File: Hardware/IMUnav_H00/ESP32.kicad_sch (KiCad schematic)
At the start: 16 parts

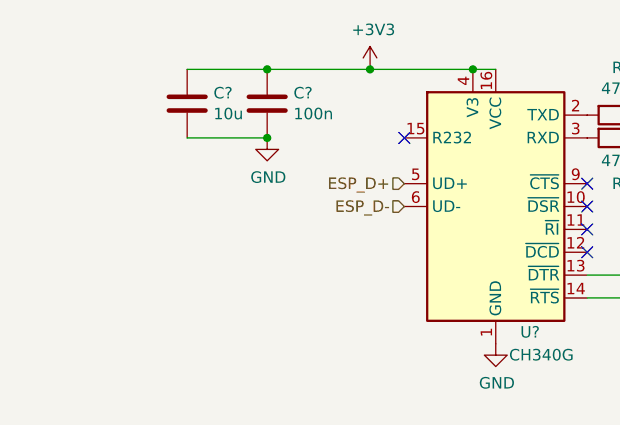
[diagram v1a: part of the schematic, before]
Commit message: Added GPS. Changes in power management.
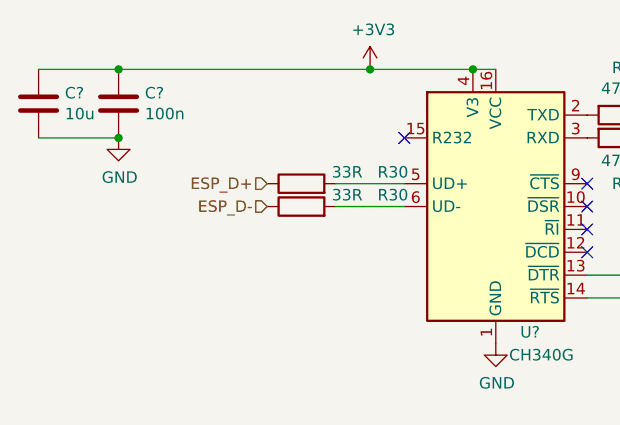
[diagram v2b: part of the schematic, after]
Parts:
- added R30 (x2): 33R, Resistor_SMD:R_0603_1608Metric, symbol Device:R
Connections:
- net ESP_D+: now also R30.1; no longer U?.5 (UD+)
- net ESP_D-: now also R30.1; no longer U?.6 (UD-)
- new net: R30.2, U?.5 (UD+)
- new net: R30.2, U?.6 (UD-)
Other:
- moved on the sheet: C?
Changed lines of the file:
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@@
   (junction (at 137.16 67.31) (diameter 0) (color 0 0 0 0)
   )
-  (junction (at 88.9 41.91) (diameter 0) (color 0 0 0 0)
+  (junction (at 72.39 41.91) (diameter 0) (color 0 0 0 0)
   )
   (junction (at 111.76 41.91) (diameter 0) (color 0 0 0 0)
@@
   (junction (at 120.65 99.06) (diameter 0) (color 0 0 0 0)
   )
-  (junction (at 88.9 49.53) (diameter 0) (color 0 0 0 0)
+  (junction (at 72.39 49.53) (diameter 0) (color 0 0 0 0)
   )
   (junction (at 120.65 105.41) (diameter 0) (color 0 0 0 0)
@@
     (stroke (width 0) (type default))
   )
+  (wire (pts (xy 96.52 57.15) (xy 104.14 57.15))
+    (stroke (width 0) (type default))
+  )
   (wire (pts (xy 177.8 41.91) (xy 177.8 119.38))
     (stroke (width 0) (type default))
@@
     (stroke (width 0) (type default))
   )
-  (wire (pts (xy 88.9 41.91) (xy 100.33 41.91))
+  (wire (pts (xy 72.39 41.91) (xy 100.33 41.91))
     (stroke (width 0) (type default))
   )
@@
     (stroke (width 0) (type default))
   )
-  (wire (pts (xy 88.9 49.53) (xy 80.01 49.53))
+  (wire (pts (xy 72.39 49.53) (xy 63.5 49.53))
     (stroke (width 0) (type default))
   )
@@
     (stroke (width 0) (type default))
   )
-  (wire (pts (xy 80.01 41.91) (xy 88.9 41.91))
+  (wire (pts (xy 63.5 41.91) (xy 72.39 41.91))
     (stroke (width 0) (type default))
   )
@@
   )
   (wire (pts (xy 120.65 99.06) (xy 120.65 105.41))
+    (stroke (width 0) (type default))
+  )
+  (wire (pts (xy 96.52 54.61) (xy 104.14 54.61))
     (stroke (width 0) (type default))
   )
@@
     (effects (font (size 1.27 1.27)) (justify left))
   )
-  (hierarchical_label "ESP_D+" (shape input) (at 104.14 54.61 180) (fields_autoplaced)
+  (hierarchical_label "ESP_D+" (shape input) (at 88.9 54.61 180) (fields_autoplaced)
     (effects (font (size 1.27 1.27)) (justify right))
   )
@@
     (effects (font (size 1.27 1.27)) (justify left))
   )
-  (hierarchical_label "ESP_D-" (shape input) (at 104.14 57.15 180) (fields_autoplaced)
+  (hierarchical_label "ESP_D-" (shape input) (at 88.9 57.15 180) (fields_autoplaced)
     (effects (font (size 1.27 1.27)) (justify right))
   )
@@
     )
   )
+  (symbol (lib_id "Device:R") (at 92.71 54.61 90) (unit 1)
+    (in_bom yes) (on_board yes) (dnp no)
+    (property "Reference" "R30" (at 102.87 53.34 90)
+      (effects (font (size 1.27 1.27)))
+    )
+    (property "Value" "33R" (at 97.79 53.34 90)
+      (effects (font (size 1.27 1.27)))
+    )
+    (property "Footprint" "Resistor_SMD:R_0603_1608Metric" (at 92.71 56.388 90)
+      (effects (font (size 1.27 1.27)) hide)
+    )
+    (property "Datasheet" "~" (at 92.71 54.61 0)
+      (effects (font (size 1.27 1.27)) hide)
+    )
+    (property "LCSC" "C23140" (at 92.71 54.61 90)
+      (effects (font (size 1.27 1.27)) hide)
+    )
+    (pin "1")
+    (pin "2")
+    (instances
+      (project "IMUnav_H00"
+        (path "/4c2dd95e-3649-4040-ab57-00df6d22e0b0/368409dd-4d9a-4752-893d-5939a8c78734"
+          (reference "R30") (unit 1)
+        )
+        (path "/4c2dd95e-3649-4040-ab57-00df6d22e0b0/61a7e487-220c-46a1-aef5-176736fd02e1"
+          (reference "R32") (unit 1)
+        )
+        (path "/4c2dd95e-3649-4040-ab57-00df6d22e0b0/bf35eb2a-37f7-4f5f-b34e-af3028cdd96b"
+          (reference "R34") (unit 1)
+        )
+      )
+    )
+  )
   (symbol (lib_id "power:GND") (at 114.3 72.39 0) (unit 1)
     (in_bom yes) (on_board yes) (dnp no)
@@
         (path "/68867493-9f89-4388-916e-56f5ada0ac5c/4ec8e228-d742-4cd8-8c0d-36879b06f45c"
           (reference "Q?") (unit 1)
+        )
+      )
+    )
+  )
+  (symbol (lib_id "Device:R") (at 92.71 57.15 90) (unit 1)
+    (in_bom yes) (on_board yes) (dnp no)
+    (property "Reference" "R30" (at 102.87 55.88 90)
+      (effects (font (size 1.27 1.27)))
+    )
+    (property "Value" "33R" (at 97.79 55.88 90)
+      (effects (font (size 1.27 1.27)))
+    )
+    (property "Footprint" "Resistor_SMD:R_0603_1608Metric" (at 92.71 58.928 90)
+      (effects (font (size 1.27 1.27)) hide)
+    )
+    (property "Datasheet" "~" (at 92.71 57.15 0)
+      (effects (font (size 1.27 1.27)) hide)
+    )
+    (property "LCSC" "C23140" (at 92.71 57.15 90)
+      (effects (font (size 1.27 1.27)) hide)
+    )
+    (pin "1")
+    (pin "2")
+    (instances
+      (project "IMUnav_H00"
+        (path "/4c2dd95e-3649-4040-ab57-00df6d22e0b0/368409dd-4d9a-4752-893d-5939a8c78734"
+          (reference "R30") (unit 1)
+        )
+        (path "/4c2dd95e-3649-4040-ab57-00df6d22e0b0/61a7e487-220c-46a1-aef5-176736fd02e1"
+          (reference "R32") (unit 1)
+        )
+        (path "/4c2dd95e-3649-4040-ab57-00df6d22e0b0/bf35eb2a-37f7-4f5f-b34e-af3028cdd96b"
+          (reference "R35") (unit 1)
         )
       )
@@
     )
   )
-  (symbol (lib_id "power:GND") (at 88.9 49.53 0) (unit 1)
-    (in_bom yes) (on_board yes) (dnp no)
-    (property "Reference" "#PWR?" (at 88.9 55.88 0)
-      (effects (font (size 1.27 1.27)) hide)
-    )
-    (property "Value" "GND" (at 89.027 53.9242 0)
-      (effects (font (size 1.27 1.27)))
-    )
-    (property "Footprint" "" (at 88.9 49.53 0)
-      (effects (font (size 1.27 1.27)) hide)
-    )
-    (property "Datasheet" "" (at 88.9 49.53 0)
+  (symbol (lib_id "power:GND") (at 72.39 49.53 0) (unit 1)
+    (in_bom yes) (on_board yes) (dnp no)
+    (property "Reference" "#PWR?" (at 72.39 55.88 0)
+      (effects (font (size 1.27 1.27)) hide)
+    )
+    (property "Value" "GND" (at 72.517 53.9242 0)
+      (effects (font (size 1.27 1.27)))
+    )
+    (property "Footprint" "" (at 72.39 49.53 0)
+      (effects (font (size 1.27 1.27)) hide)
+    )
+    (property "Datasheet" "" (at 72.39 49.53 0)
       (effects (font (size 1.27 1.27)) hide)
     )
@@
     )
   )
-  (symbol (lib_id "Device:C") (at 80.01 45.72 0) (unit 1)
-    (in_bom yes) (on_board yes) (dnp no)
-    (property "Reference" "C?" (at 82.931 44.5516 0)
-      (effects (font (size 1.27 1.27)) (justify left))
-    )
-    (property "Value" "10u" (at 82.931 46.863 0)
-      (effects (font (size 1.27 1.27)) (justify left))
-    )
-    (property "Footprint" "Capacitor_SMD:C_0603_1608Metric" (at 80.9752 49.53 0)
-      (effects (font (size 1.27 1.27)) hide)
-    )
-    (property "Datasheet" "~" (at 80.01 45.72 0)
-      (effects (font (size 1.27 1.27)) hide)
-    )
-    (property "LCSC" "C19702" (at 80.01 45.72 0)
+  (symbol (lib_id "Device:C") (at 63.5 45.72 0) (unit 1)
+    (in_bom yes) (on_board yes) (dnp no)
+    (property "Reference" "C?" (at 66.421 44.5516 0)
+      (effects (font (size 1.27 1.27)) (justify left))
+    )
+    (property "Value" "10u" (at 66.421 46.863 0)
+      (effects (font (size 1.27 1.27)) (justify left))
+    )
+    (property "Footprint" "Capacitor_SMD:C_0603_1608Metric" (at 64.4652 49.53 0)
+      (effects (font (size 1.27 1.27)) hide)
+    )
+    (property "Datasheet" "~" (at 63.5 45.72 0)
+      (effects (font (size 1.27 1.27)) hide)
+    )
+    (property "LCSC" "C19702" (at 63.5 45.72 0)
       (effects (font (size 1.27 1.27)) hide)
     )
@@
     )
   )
-  (symbol (lib_id "Device:C") (at 88.9 45.72 0) (unit 1)
-    (in_bom yes) (on_board yes) (dnp no)
-    (property "Reference" "C?" (at 91.821 44.5516 0)
-      (effects (font (size 1.27 1.27)) (justify left))
-    )
-    (property "Value" "100n" (at 91.821 46.863 0)
-      (effects (font (size 1.27 1.27)) (justify left))
-    )
-    (property "Footprint" "Capacitor_SMD:C_0603_1608Metric" (at 89.8652 49.53 0)
-      (effects (font (size 1.27 1.27)) hide)
-    )
-    (property "Datasheet" "~" (at 88.9 45.72 0)
-      (effects (font (size 1.27 1.27)) hide)
-    )
-    (property "LCSC" "C14663" (at 88.9 45.72 0)
-      (effects (font (size 1.27 1.27)) hide)
-    )
+  (symbol (lib_id "Device:C") (at 72.39 45.72 0) (unit 1)
+    (in_bom yes) (on_board yes) (dnp no)
+    (property "Reference" "C?" (at 75.311 44.5516 0)
+      (effects (font (size 1.27 1.27)) (justify left))
+    )
+    (property "Value" "100n" (at 75.311 46.863 0)
+      (effects (font (size 1.27 1.27)) (justify left))
+    )
+    (property "Footprint" "Capacitor_SMD:C_0603_1608Metric" (at 73.3552 49.53 0)
+      (effects (font (size 1.27 1.27)) hide)
+    )
+    (property "Datasheet" "~" (at 72.39 45.72 0)
+      (effects (font (size 1.27 1.27)) hide)
+    )
+    (property "LCSC" "C14663" (at 72.39 45.72 0)
+      (effects (font (size 1.27 1.27)) hide)
+    )

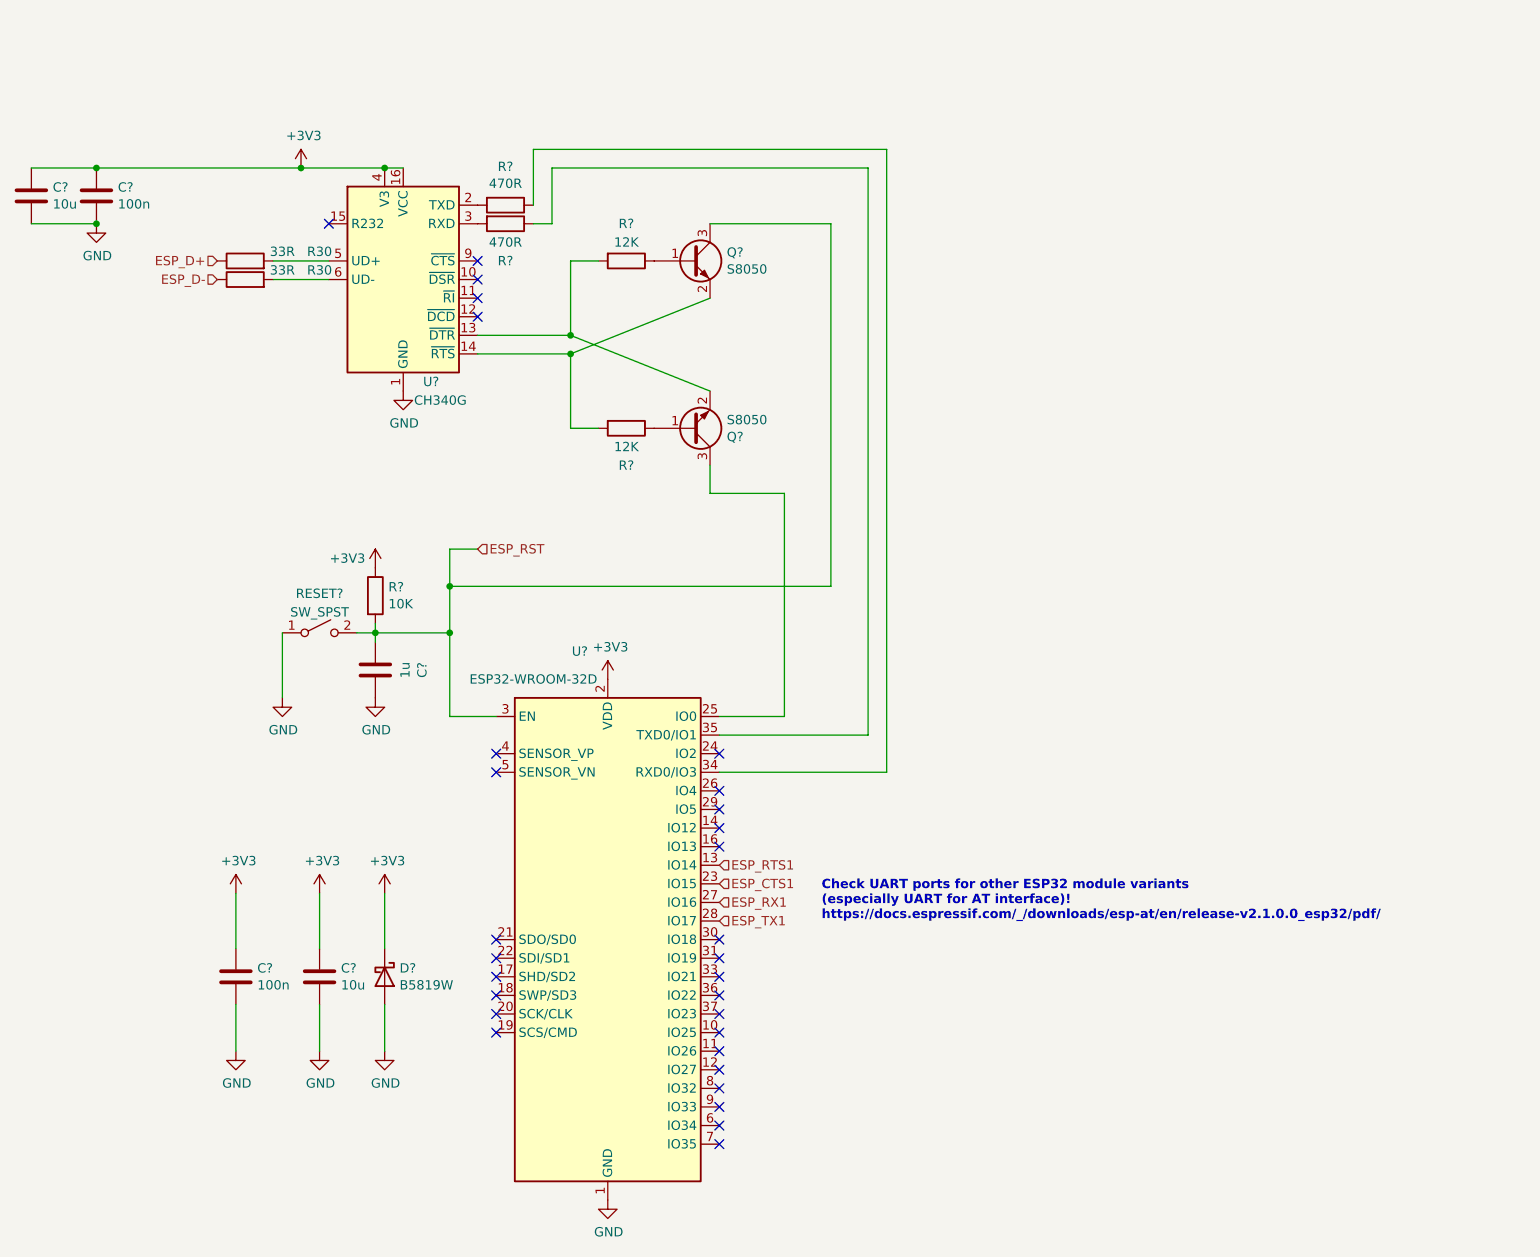
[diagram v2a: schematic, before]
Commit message: Added uSD card, changed ESP module to C3-MINI, changed MCU to STM32F4
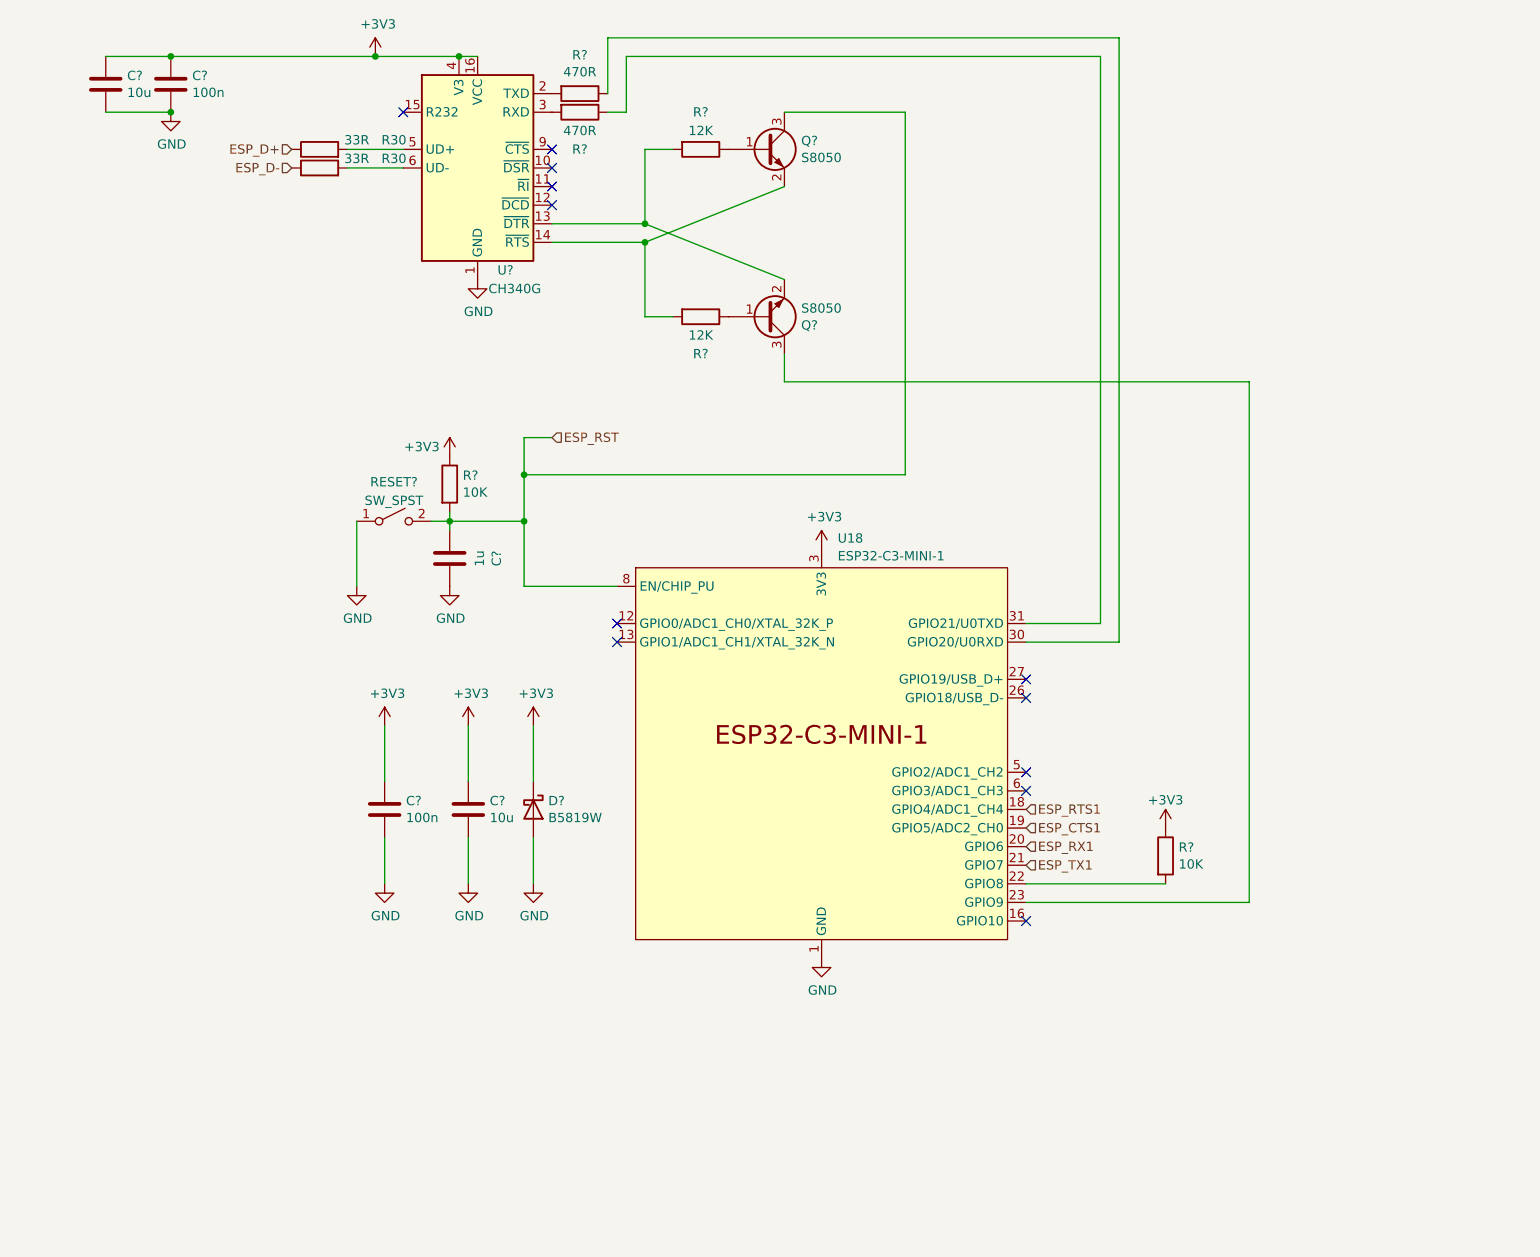
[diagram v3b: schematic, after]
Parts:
- removed U?: ESP32-WROOM-32D, RF_Module:ESP32-WROOM-32, symbol RF_Module:ESP32-WROOM-32D
- added R?: 10K, Resistor_SMD:R_0603_1608Metric, symbol Device:R
- added U18: ESP32-C3-MINI-1, PCM_Espressif:ESP32-C3-MINI-1, symbol PCM_Espressif:ESP32-C3-MINI-1
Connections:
- net +3V3: now also R?.1, U18.3 (3V3)
- net ESP_CTS1: now also U18.19 (GPIO5/ADC2_CH0)
- net ESP_RST: now also U18.8 (EN/CHIP_PU)
- net ESP_RTS1: now also U18.18 (GPIO4/ADC1_CH4)
- net ESP_RX1: now also U18.20 (GPIO6)
- net ESP_TX1: now also U18.21 (GPIO7)
- net GND: now also U18.1 (GND), U18.11 (GND), U18.14 (GND), U18.2 (GND), U18.36 (GND), U18.37 (GND), U18.38 (GND), U18.39 (GND), U18.40 (GND), U18.41 (GND), U18.42 (GND), U18.43 (GND), U18.44 (GND), U18.45 (GND), U18.46 (GND), U18.47 (GND), U18.48 (GND), U18.49 (GND), U18.50 (GND), U18.51 (GND), U18.52 (GND), U18.53 (GND)
- net at R?.1: now also U18.30 (GPIO20/U0RXD)
- net at Q?.3 (C): now also U18.23 (GPIO9)
- net at R?.1: now also U18.31 (GPIO21/U0TXD)
- new net: R?.2, U18.22 (GPIO8)
- no-connect marks 30 -> 12
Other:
- note removed: "Check UART ports for other ESP32 module variants (especially UART for AT interface)! https://docs.espressif.com/_/downloads/esp-at/en/release-v2.1.0.0_esp32/pdf/"
- moved on the sheet: C?, D?, Q?, R30, R?, RESET?, U?
